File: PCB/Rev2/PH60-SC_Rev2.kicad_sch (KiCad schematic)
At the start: 43 parts, among them J1 Conn_01x02_Pin, J3 USB_C_Receptacle_USB2.0_14P, J4 Conn_01x02_Pin, U1 nRF52840, X2 32.768kHz, X3 Crystal_Generic

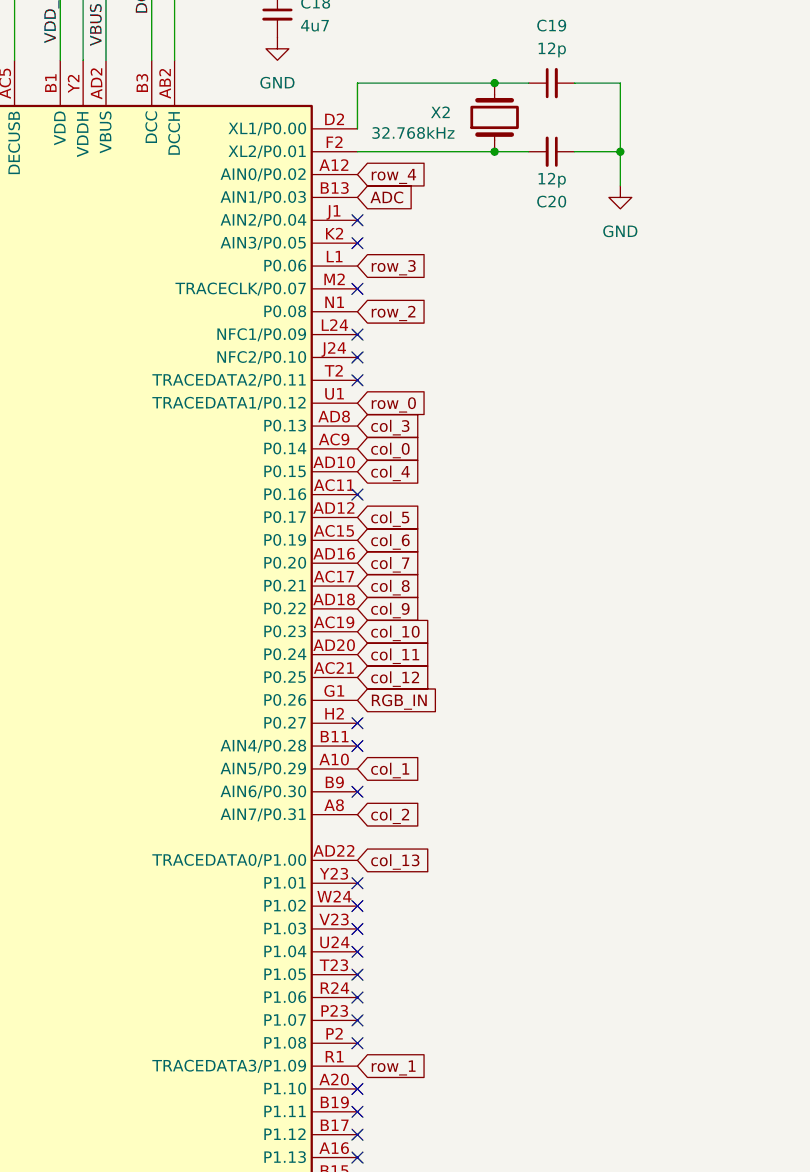
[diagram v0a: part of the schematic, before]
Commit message: Modification of RGB matrix schematic, modification of button matrix schematic, and confirmation of approximate wiring.
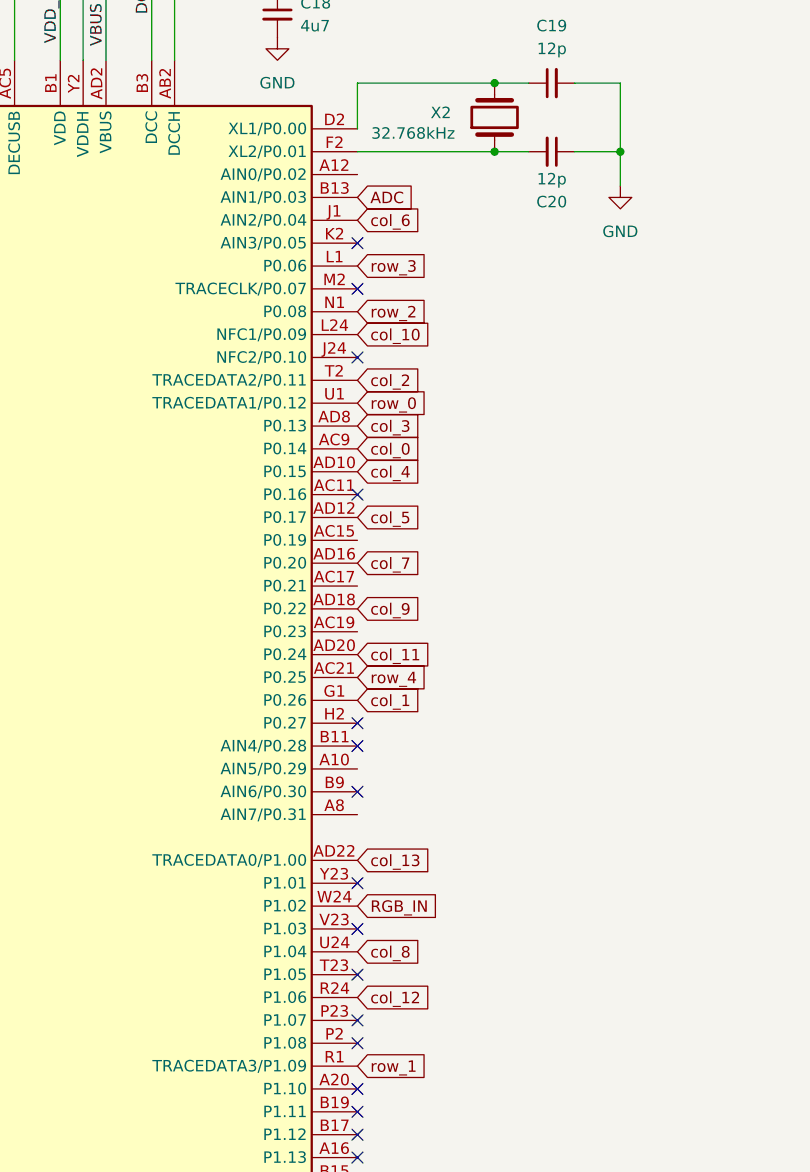
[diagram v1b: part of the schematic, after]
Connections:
- net RGB_IN: now also U1.W24 (P1.02); no longer U1.G1 (P0.26)
- net col_1: now also U1.G1 (P0.26); no longer U1.A10 (AIN5/P0.29)
- net col_10: now also U1.L24 (NFC1/P0.09); no longer U1.AC19 (P0.23)
- net col_12: now also U1.R24 (P1.06); no longer U1.AC21 (P0.25)
- net col_2: now also U1.T2 (TRACEDATA2/P0.11); no longer U1.A8 (AIN7/P0.31)
- net col_6: now also U1.J1 (AIN2/P0.04); no longer U1.AC15 (P0.19)
- net col_8: now also U1.U24 (P1.04); no longer U1.AC17 (P0.21)
- net row_4: now also U1.AC21 (P0.25); no longer U1.A12 (AIN0/P0.02)
- no-connect marks 24 -> 18

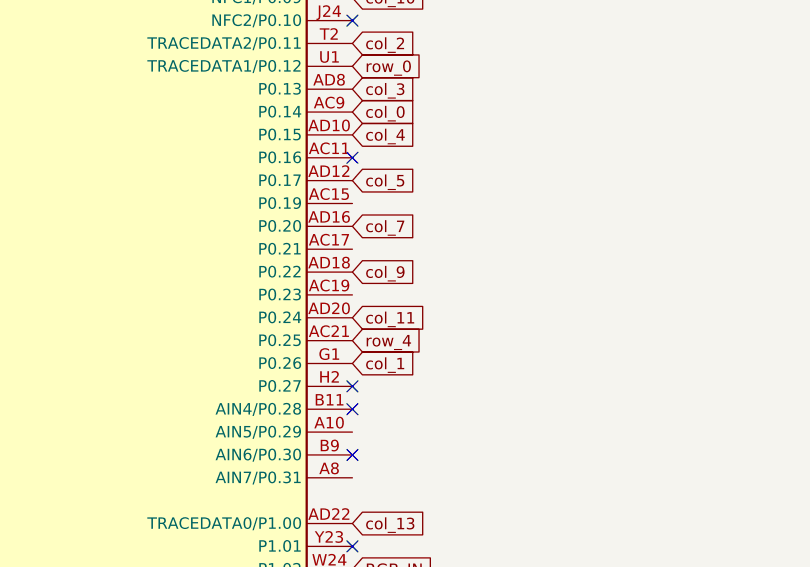
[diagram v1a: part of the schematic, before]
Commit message: The basic layout is complete, and a full DRC scan is underway. RGB signal line interference needs to be considered. The battery connector has not yet been selected.
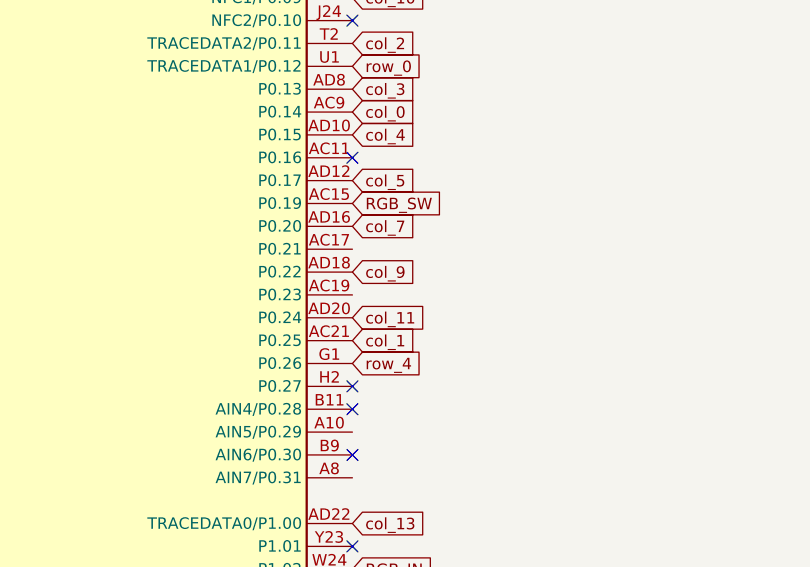
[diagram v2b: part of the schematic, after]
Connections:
- net col_1: now also U1.AC21 (P0.25); no longer U1.G1 (P0.26)
- net row_4: now also U1.G1 (P0.26); no longer U1.AC21 (P0.25)
- net RGB_SW: now reaches U1.AC15 (P0.19)
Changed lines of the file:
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@@
+		)
+	)
+	(global_label "col_1"
+		(shape input)
+		(at 256.54 147.32 0)
+		(fields_autoplaced yes)
+		(effects
+			(font
+				(size 1.27 1.27)
+			)
+			(justify left)
+		)
+		(property "Intersheetrefs" "${INTERSHEET_REFS}"
+			(at 264.6051 147.32 0)
+			(effects
+				(font
+					(size 1.27 1.27)
+				)
+				(justify left)
+				(hide yes)
+			)
 		)
 	)
@@
 		)
 	)
-	(global_label "col_1"
+	(global_label "row_4"
 		(shape input)
 		(at 256.54 149.86 0)
@@
 		)
 		(property "Intersheetrefs" "${INTERSHEET_REFS}"
-			(at 264.6051 149.86 0)
+			(at 264.968 149.86 0)
 			(effects
 				(font
@@
 		)
 	)
-	(global_label "row_4"
-		(shape input)
-		(at 256.54 147.32 0)
-		(fields_autoplaced yes)
-		(effects
-			(font
-				(size 1.27 1.27)
-			)
-			(justify left)
-		)
-		(property "Intersheetrefs" "${INTERSHEET_REFS}"
-			(at 264.968 147.32 0)
-			(effects
-				(font
-					(size 1.27 1.27)
-				)
-				(justify left)
-				(hide yes)
-			)
-		)
-	)
 	(global_label "CHRG"
 		(shape input)
@@
 			(effects
 				(font
+					(size 1.27 1.27)
+				)
+				(justify left)
+				(hide yes)
+			)
+		)
+	)
+	(global_label "RGB_SW"
+		(shape input)
+		(at 256.54 132.08 0)
+		(fields_autoplaced yes)
+		(effects
+			(font
+				(size 1.27 1.27)
+			)
+			(justify left)
+		)
+		(property "Intersheetrefs" "${INTERSHEET_REFS}"
+			(at 266.9637 132.08 0)
+			(effects
+				(font

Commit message: layout and drc
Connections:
- net col_1: now also U1.B11 (AIN4/P0.28); no longer U1.AC21 (P0.25)
- no-connect marks 18 -> 15

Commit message: layout and  Routing adjustment
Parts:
- renumbered C12 to C1, C8 to C10, C9 to C12, C10 to C13, C2 to C14, C4 to C15, C1 to C16, C3 to C17, C5 to C18, C6 to C19, C14 to C2, C7 to C20, C16 to C3, C13 to C4, C15 to C5, C17 to C6, C18 to C7, C19 to C8, C20 to C9, D65 to D1, H4 to H2, H2 to H3, H5 to H4, H3 to H5, J3 to J1, J4 to J2, J1 to J3, L4 to L1, L3 to L2, L1 to L3, L2 to L4, R5 to R1, R6 to R2, R1 to R3, R3 to R4, R4 to R5, X2 to X1, X3 to X2
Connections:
- net ADC: now also U1.A12 (AIN0/P0.02); no longer U1.B13 (AIN1/P0.03)
